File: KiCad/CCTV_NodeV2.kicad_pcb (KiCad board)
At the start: 2 copper layers, 93.6 x 93.6 mm, 9 parts, among them J1 Solar 6V/10W, J2 Battery (ext, 2× 18650 ||), U1 CN3791, U2 TC4056A_BMS, U3 MT3608, U4 ESP32-S3-DevKitC-1 N16R8, U5 OV7670

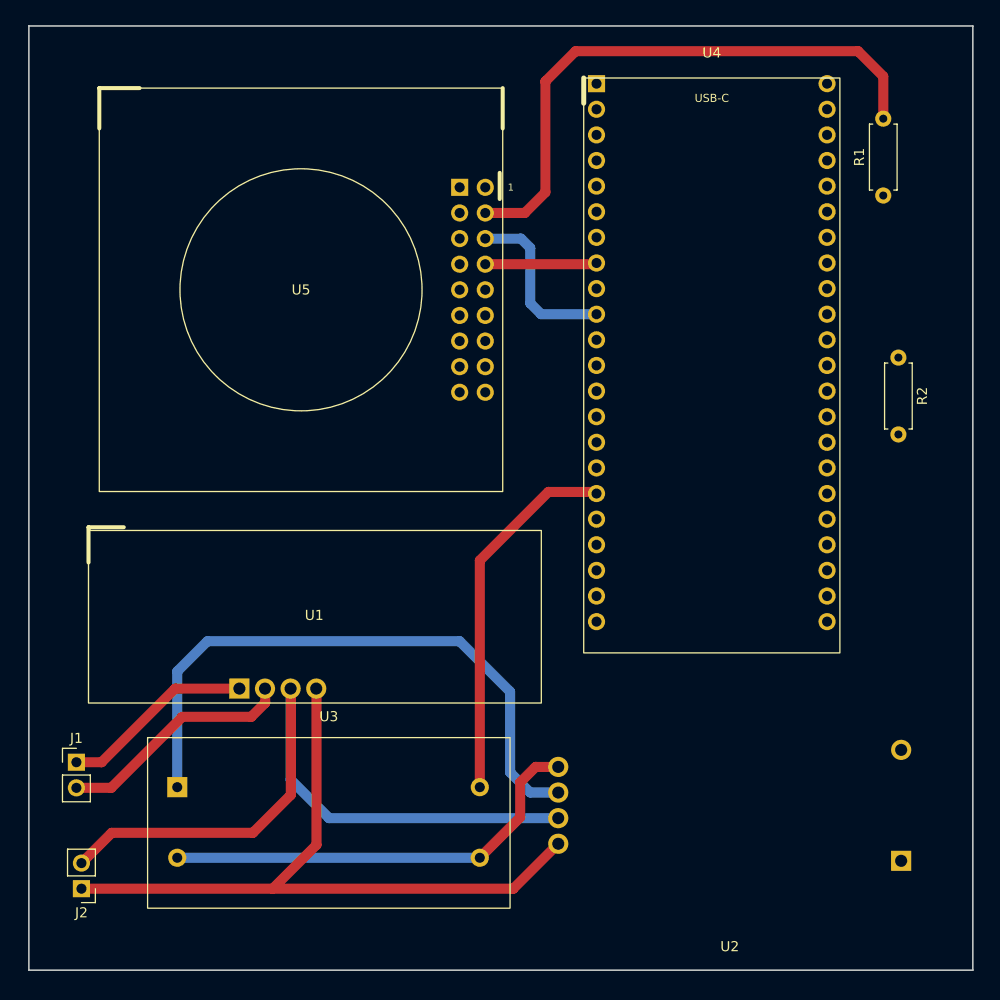
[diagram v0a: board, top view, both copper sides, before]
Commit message: Save PCB layout, project settings and DRC report
KiCad/CCTV_NodeV2.kicad_pcb:
- PCB layout updated in pcbnew (component placement, footprint
  refreshes, routing changes)

KiCad/CCTV_NodeV2.kicad_pro:
- Project settings updated: min_text_height 0.8→0.5mm (resolved
  silk text height DRC warnings), min_via_diameter 1.0→0.6mm

KiCad/DRC.rpt:
- Updated DRC report from latest run
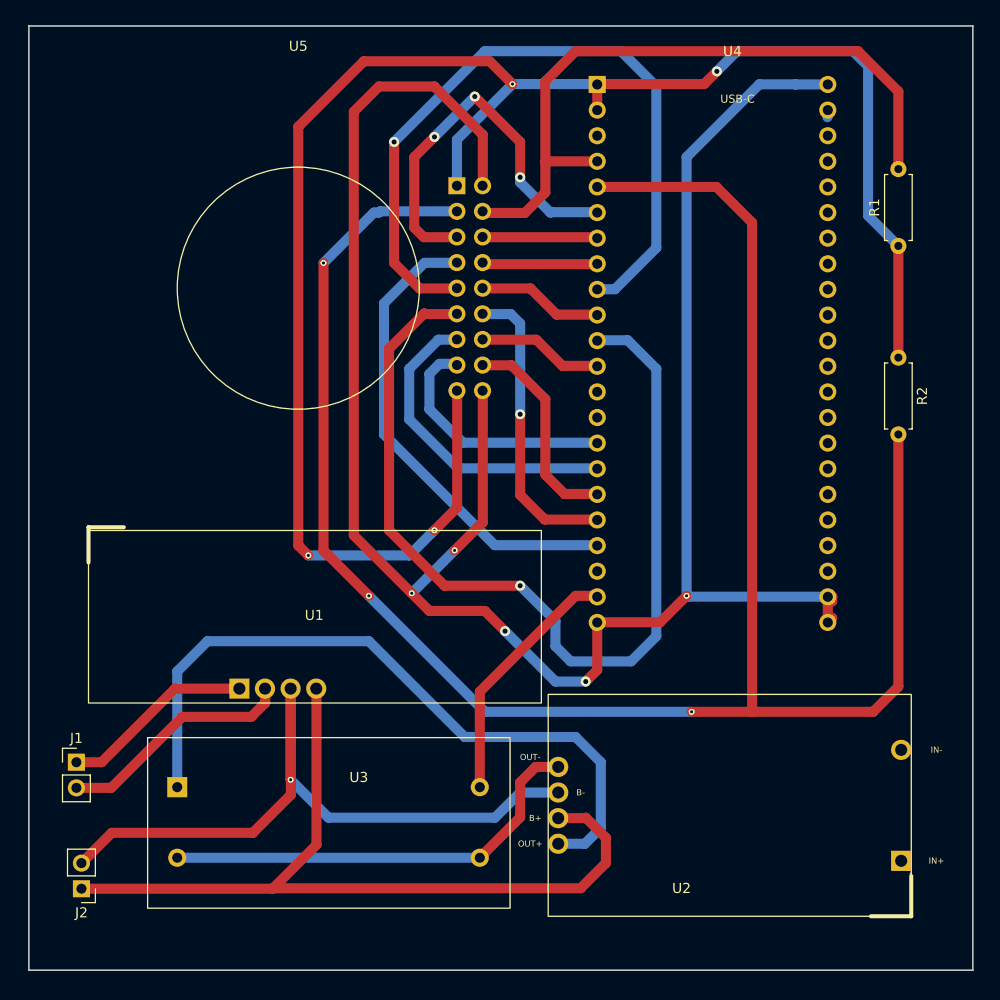
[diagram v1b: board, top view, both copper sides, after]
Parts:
- moved R1 5.22 mm to (103.0, 54.3)
- moved U5 0.31 mm to (60.5, 58.5)
- moved U4 0.11 mm to (84.6, 66.2)
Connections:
- U4 pad 10: unconnected-(U4-GPIO17_D6-Pad10) -> /CAM_D6
- U4 pad 11: unconnected-(U4-GPIO18_D5-Pad11) -> /CAM_D5
- U4 pad 12: unconnected-(U4-GPIO8_D2-Pad12) -> /CAM_D2
- U4 pad 15: unconnected-(U4-GPIO9_D1-Pad15) -> /CAM_D1
- U4 pad 16: unconnected-(U4-GPIO10_D3-Pad16) -> /CAM_D3
- U4 pad 17: unconnected-(U4-GPIO11_D0-Pad17) -> /CAM_D0
- U4 pad 18: unconnected-(U4-GPIO12_D4-Pad18) -> /CAM_D4
- U4 pad 19: unconnected-(U4-GPIO13_PCLK-Pad19) -> /PCLK
- U4 pad 2: unconnected-(U4-3V3_2-Pad2) -> +3V3
- U4 pad 4: unconnected-(U4-GPIO4_SIOD-Pad4) -> /SIOD
- U4 pad 5: unconnected-(U4-GPIO5_SIOC-Pad5) -> /SIOC
- U4 pad 6: unconnected-(U4-GPIO6_VSYNC-Pad6) -> /VSYNC
- U4 pad 7: unconnected-(U4-GPIO7_HREF-Pad7) -> /HREF
- U4 pad 8: unconnected-(U4-GPIO15_XCLK-Pad8) -> /XCLK
- U4 pad 9: unconnected-(U4-GPIO16_D7-Pad9) -> /CAM_D7
- U5 pad 17: unconnected-(U5-RESET-Pad17) -> +3V3
- U5 pad 18: unconnected-(U5-PWDN-Pad18) -> GND
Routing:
- net GND: track 0.00 -> 210.4 mm, vias 0 -> 5
- net /SIOC: track 0.00 -> 198.9 mm, vias 0 -> 3
- net +3V3: track 0.00 -> 178.5 mm, vias 0 -> 4
- net /CAM_D5: track 0.00 -> 93.7 mm, vias 0 -> 1
- net /CAM_D7: track 0.00 -> 73.6 mm, vias 0 -> 1
- net /PCLK: track 0.00 -> 47.5 mm
- net /VSYNC: track 0.00 -> 39.3 mm, vias 0 -> 3
- net /CAM_D3: track 0.00 -> 31.5 mm
- net /CAM_D4: track 0.00 -> 29.6 mm, vias 0 -> 1
- net /CAM_D1: track 0.00 -> 24.6 mm
- net /CAM_D0: track 0.00 -> 20.9 mm
- net /CAM_D2: track 0.00 -> 12.3 mm
- net /CAM_D6: track 0.00 -> 12.3 mm
- net BATT+: track 70.8 -> 82.8 mm
- net +5V: track 36.9 -> 25.0 mm
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
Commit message: Round PCB outline to 95x95mm and add 4 M3 mounting holes
Board outline (Edge.Cuts):
  Before: (16.788733, 32.5) to (110.383416, 126.116556) ≈ 93.6 x 93.6 mm
  After:  (16, 32)          to (111, 127)               = 95 x 95 mm

4 x M3 mounting holes (NPTH, 3.2mm drill), 3.5mm inset from corners:
  Top-left     : (19.5,   35.5)
  Top-right    : (107.5,  35.5)
  Bottom-left  : (19.5,  123.5)
  Bottom-right : (107.5, 123.5)

Hole spacing:
  Horizontal: 107.5 - 19.5 = 88 mm centre-to-centre
  Vertical:   123.5 - 35.5 = 88 mm centre-to-centre
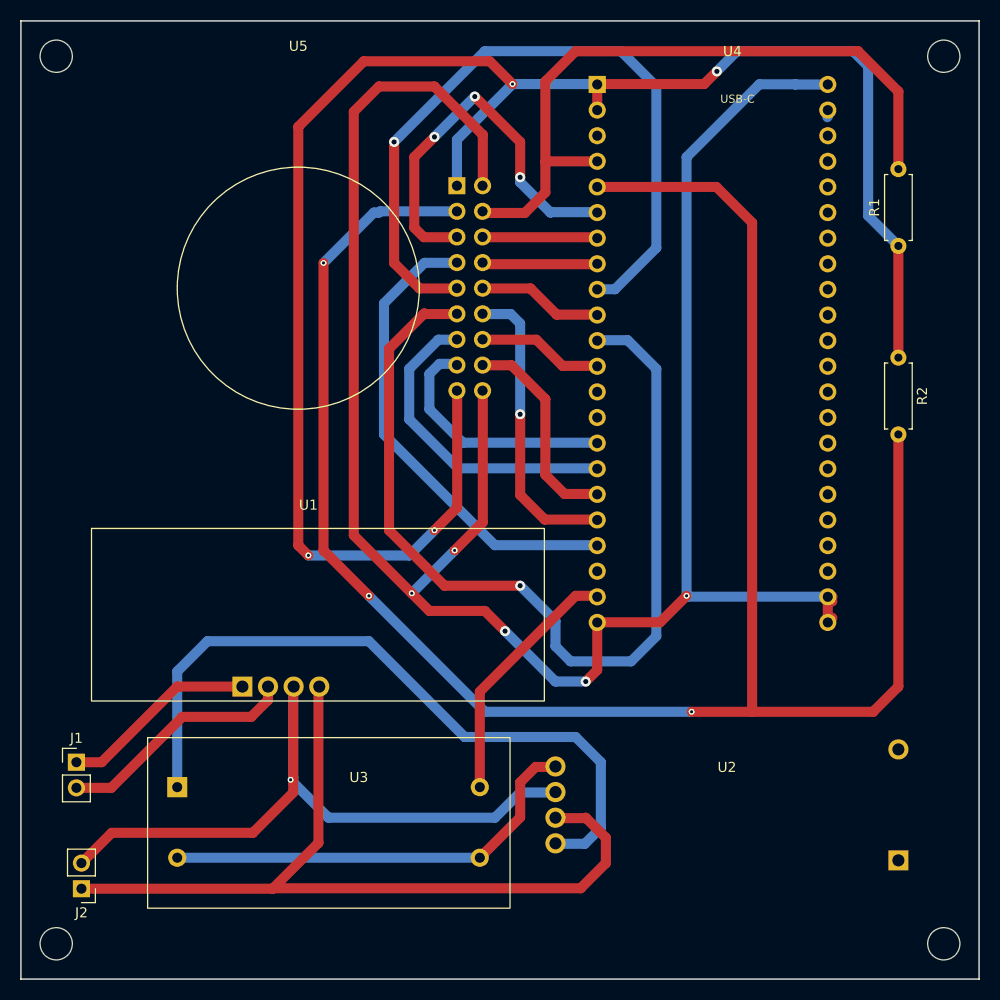
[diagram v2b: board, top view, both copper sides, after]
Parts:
- added ?: , MountingHole:MountingHole_3.2mm, F.Cu at (19.5, 35.5)
- added ?: , MountingHole:MountingHole_3.2mm, F.Cu at (107.5, 35.5)
- added ?: , MountingHole:MountingHole_3.2mm, F.Cu at (19.5, 123.5)
- added ?: , MountingHole:MountingHole_3.2mm, F.Cu at (107.5, 123.5)
- moved U1 0.36 mm to (40.5, 90.5)
- moved U2 0.28 mm to (86.0, 109.7)
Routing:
- net BATT+: track 82.8 -> 83.4 mm
- net /SOLAR-: track 23.6 -> 24.3 mm
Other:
- board size 93.6 x 93.6 mm -> 95 x 95 mm
